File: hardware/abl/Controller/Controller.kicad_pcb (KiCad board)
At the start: 4 copper layers, 56.2 x 74 mm, 29 parts, among them IC1 LSF0204PWJ, IC2 FXL6408UMX, IC3 VEML6040A3OG, IC4 FXL6408UMX, J1 SFW20S-2STE1LF, J2 Conn_02x03_Odd_Even, J3 Conn_02x03_Odd_Even, J4 PRT-14417, J5 Conn_02x04_Odd_Even, Q2 AO3401A, Q4 AO3401A, U1 INA219AxD

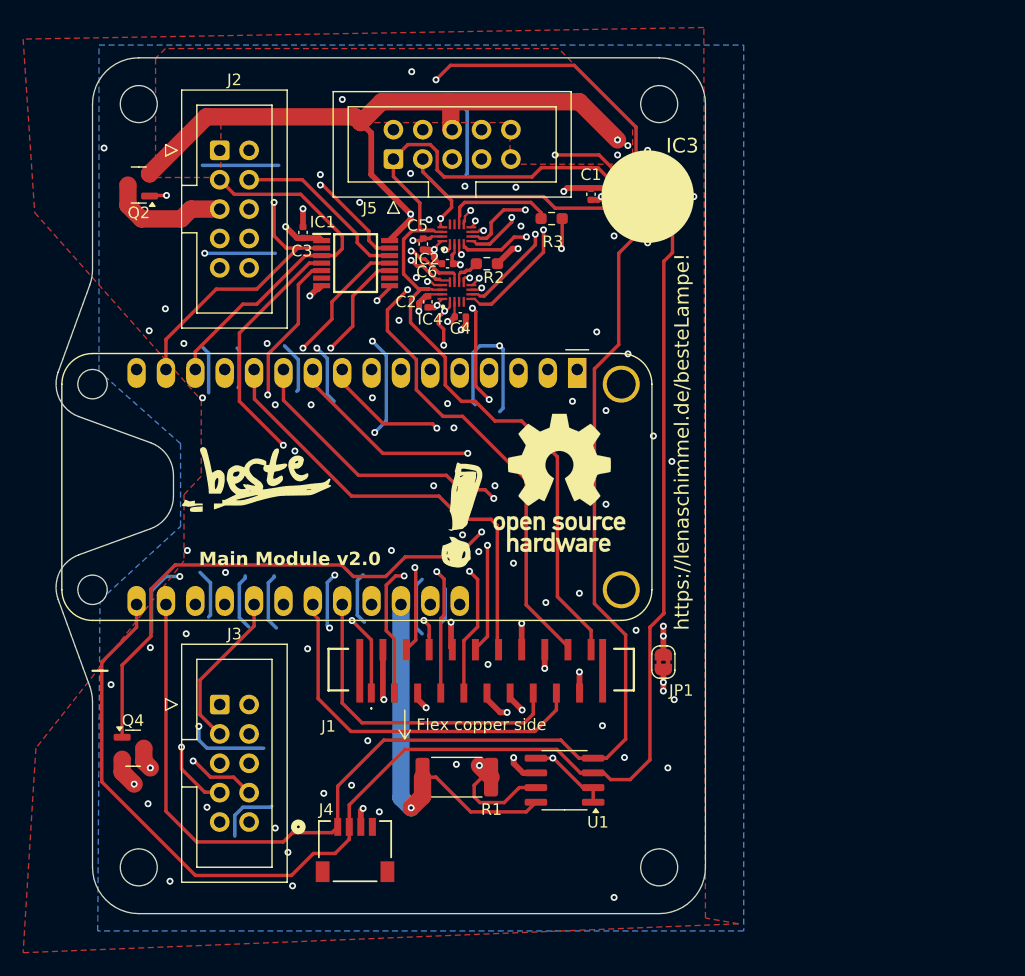
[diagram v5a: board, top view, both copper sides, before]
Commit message: Move light sensor closer to the center, many microoptimizazions.
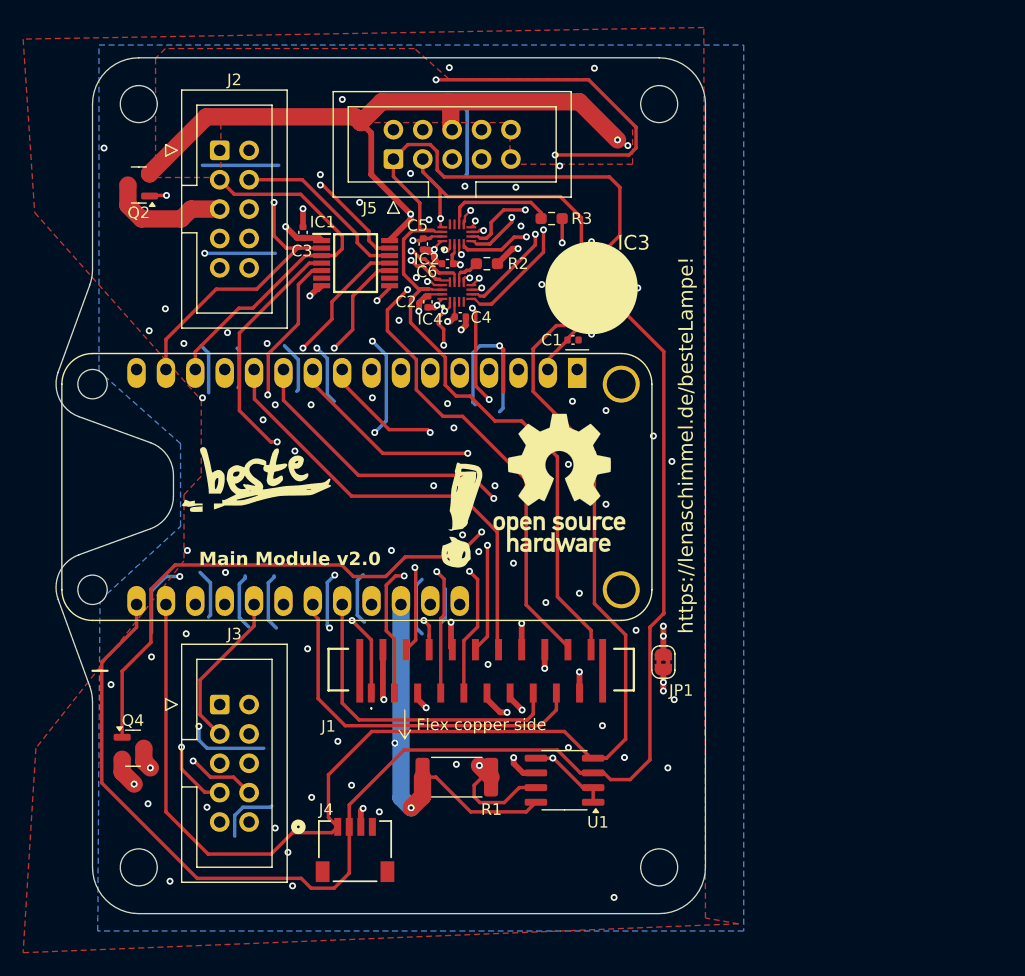
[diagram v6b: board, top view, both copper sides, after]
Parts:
- moved C1 12.7 mm to (104.5, 75.4), turned to 0 degrees
- moved IC3 9.27 mm to (106.2, 71.9)
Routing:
- net +3.3V: track 154.8 -> 123.9 mm, vias 11 -> 10
- net +5V: track 191.3 -> 168.7 mm, vias 9 -> 8
- net GND: track 240.1 -> 246.3 mm, vias 87 -> 91
- net /FX_5_6: track 77.5 -> 74.9 mm
- net /SDA: track 213.9 -> 214.6 mm
- net /i5: track 36.3 -> 35.7 mm

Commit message: Metadata and minor cleanup, documentation and typo fix.
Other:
- board text added: "ABL Controller v1.0"
- board text removed: "Main Module v2.0"

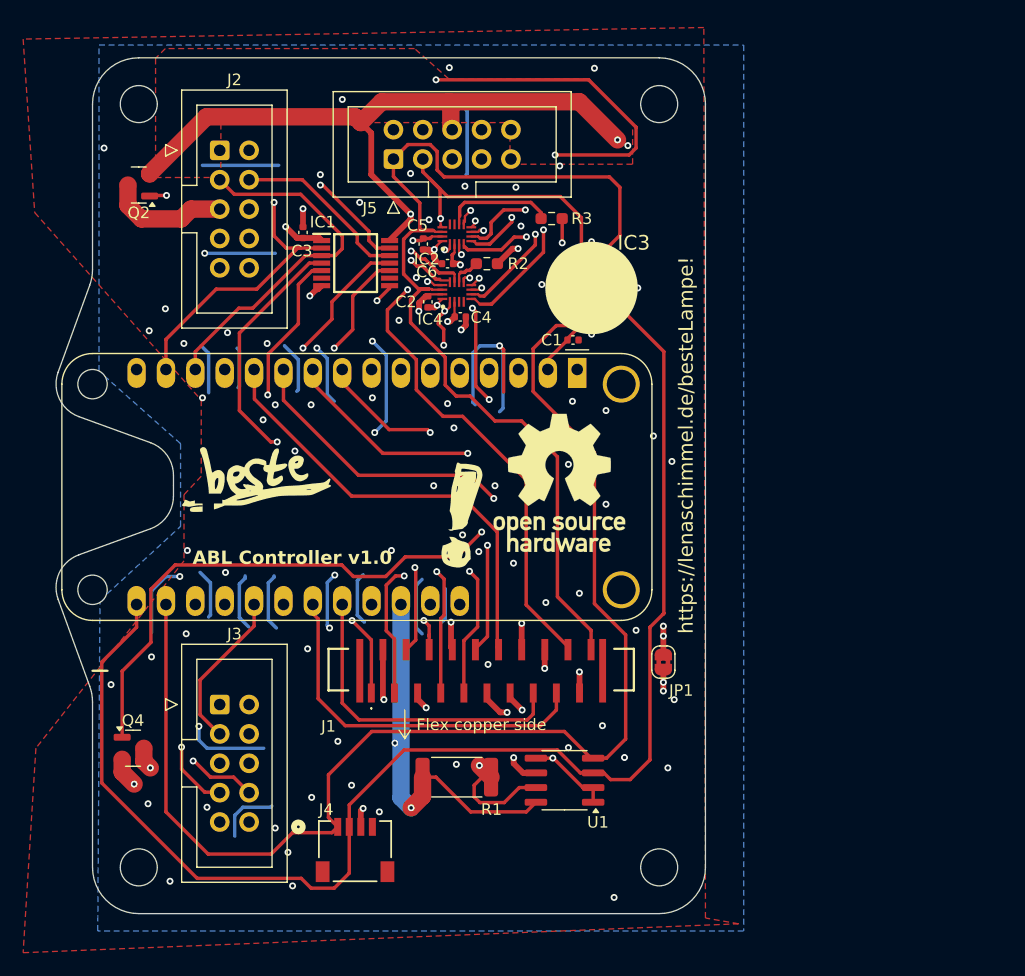
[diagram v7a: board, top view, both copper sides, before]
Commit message: Controller: Swivel GPIOs 16, 21, 22, 25 to be compatible with all three feather variants and add README.
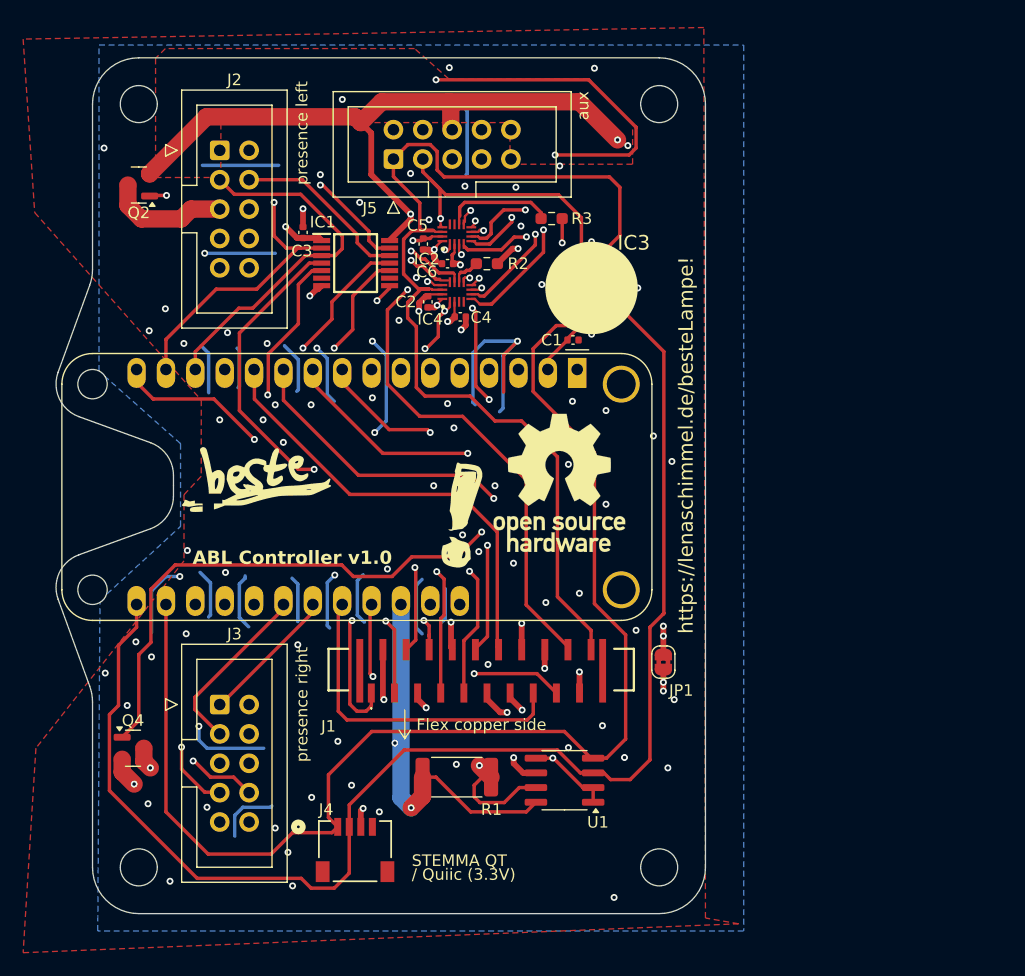
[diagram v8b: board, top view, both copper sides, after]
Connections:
- A1 pad 16: unconnected-(A1-SPARE-Pad16) -> /GP_INT
- A1 pad 21: /RX_R -> unconnected-(A1-D2-Pad21)
- A1 pad 22: /TX_R -> /RX_R
- A1 pad 23: /ALERT -> /TX_R
- A1 pad 25: /GP_INT -> /ALERT
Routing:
- net +3.3V: track 123.9 -> 114.1 mm
- net /GP_INT: track 38.5 -> 47.3 mm, vias 3 -> 4
- net /ALERT: track 32.0 -> 23.7 mm, vias 0 -> 2
- net GND: track 246.3 -> 240.7 mm, vias 91 -> 92
- net (no net): track 0.00 -> 3.96 mm
- net /i4: track 29.5 -> 33.3 mm
- net /TX_R: track 45.9 -> 48.7 mm
- net /RX_R: track 45.6 -> 47.1 mm
- net /SDA: track 214.6 -> 215.8 mm
- net /SCL: track 190.2 -> 191.4 mm
- net /TX_R_5: track 55.1 -> 56.1 mm
- net /FX_5_2: track 69.1 -> 70.0 mm
- net /EN_LED: track 27.8 -> 28.7 mm
- net /i3: track 29.6 -> 28.8 mm
- net /RX_R_5: track 45.7 -> 46.3 mm
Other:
- board text added: "/ Quiic (3.3V)"
- board text added: "STEMMA QT"
- board text added: "aux"
- board text added: "presence left"
- board text added: "presence right"
